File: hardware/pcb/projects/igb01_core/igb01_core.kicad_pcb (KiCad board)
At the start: 2 copper layers, 80 x 80 mm, 115 parts, among them J1 BAT_CON, J10 STMP157_GPIO2, J11 STMP157_GPIO3, J12 JTAG, J13 STMP157_GPIO4, J14 Micro_SD_Card, J15 PWR_ON_CON, J16 STMP157_GPIO5, J17 USB_CONN, J18 FPA-VZA2-15-LF, J19 I2C, J2 STMP157_GPIO1, J20 STMP157_GPIO6, J21 Conn_01x13, J3 LEFT_CON, J4 RIGHT_CON, J5 IGB_PREV, J6 IGB_NEXT, J7 IGB2_NEXT, J8 IGB3_NEXT, J9 CAN, SW1 SW_DIP_x04, SW2 SW_Push, SW3 SW_Push, U1 SIT1050T, U2 TPS2041B, U3 W25Q128JVS, U4 AK4619

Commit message: update core board sch&pcb
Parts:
- C4, C6: footprint Capacitor_SMD:C_0805_2012Metric -> Capacitor_SMD:C_0402_1005Metric
- moved U2 67.3 mm to (132.2, 89.2)
- moved C6 66.0 mm to (128.1, 85.1)
- moved C8 63.5 mm to (129.9, 86.5)
- moved R20 62.9 mm to (129.0, 90.2)
- moved C7 60.5 mm to (133.3, 86.5), turned to 180 degrees
- moved R30 57.4 mm to (159.4, 126.8)
- moved R31 56.5 mm to (159.4, 127.8)
- moved C4 47.2 mm to (151.9, 98.5)
- moved R15 47.0 mm to (151.4, 100.0)
- moved R2 46.8 mm to (151.1, 85.7)
- moved R12 44.1 mm to (153.8, 99.5), turned to -90 degrees
- moved R3 42.4 mm to (128.1, 68.1)
- moved R4 39.2 mm to (131.6, 68.1), turned to 180 degrees
- moved R8 38.8 mm to (150.2, 68.1)
- moved R28 26.9 mm to (160.4, 129.9), turned to 90 degrees
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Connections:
- J10 pad 15: /USB_OTG_FS_ID -> unconnected-(J10-Pin_15-Pad15)
- J10 pad 30: /SPI2_MOSI -> unconnected-(J10-Pin_30-Pad30)
- J11 pad 18: /GPIO_CLOCK_OUT -> unconnected-(J11-Pin_18-Pad18)
- J11 pad 20: /GPIO_RESET_OUT -> unconnected-(J11-Pin_20-Pad20)
- J11 pad 40: /SPI4_NSS -> unconnected-(J11-Pin_40-Pad40)
- J13 pad 33: /UART7_RX -> unconnected-(J13-Pin_33-Pad33)
- J13 pad 35: /UART7_TX -> unconnected-(J13-Pin_35-Pad35)
- J16 pad 25: /SPI4_GPIO_CS1 -> unconnected-(J16-Pin_25-Pad25)
- J16 pad 27: /SPI4_SCK -> unconnected-(J16-Pin_27-Pad27)
- J16 pad 28: /SPI2_NSS -> unconnected-(J16-Pin_28-Pad28)
- J16 pad 29: /SPI4_MISO -> unconnected-(J16-Pin_29-Pad29)
- J16 pad 31: /SPI4_MOSI -> unconnected-(J16-Pin_31-Pad31)
- J17 pad 1: /USB1_D+ -> /USB2_D+
- J17 pad 2: /USB1_D- -> /USB2_D-
- J17 pad 5: /USB2_D+ -> /USB1_D+
- J17 pad 6: /USB2_D- -> /USB1_D-
- J2 pad 19: unconnected-(J2-Pin_19-Pad19) -> /SPI6_MISO
- J2 pad 23: unconnected-(J2-Pin_23-Pad23) -> /SPI6_NSS
- J2 pad 24: unconnected-(J2-Pin_24-Pad24) -> /SPI6_MOSI
- J2 pad 25: unconnected-(J2-Pin_25-Pad25) -> /GPIO1
- J2 pad 26: unconnected-(J2-Pin_26-Pad26) -> /SPI6_SCK
- J2 pad 30: unconnected-(J2-Pin_30-Pad30) -> /SPI2_MISO
- J2 pad 35: unconnected-(J2-Pin_35-Pad35) -> /SPI2_CS_GPIO
- J2 pad 37: unconnected-(J2-Pin_37-Pad37) -> /GPIO_CLOCK_OUT
- J2 pad 39: unconnected-(J2-Pin_39-Pad39) -> /GPIO_RESET_OUT
- J2 pad 40: unconnected-(J2-Pin_40-Pad40) -> /SPI2_MOSI
- J20 pad 10: unconnected-(J20-Pin_10-Pad10) -> /LCD_TP_RST
- J20 pad 12: /LCD_TP_RST -> /LCD_TP_INT
- J20 pad 14: /LCD_TP_INT -> /UART8_TX
- J20 pad 15: unconnected-(J20-Pin_15-Pad15) -> /UART8_RX
- J20 pad 36: unconnected-(J20-Pin_36-Pad36) -> /I2C1_SDA
- J20 pad 40: /I2C1_SDA -> unconnected-(J20-Pin_40-Pad40)
- J3 pad 10: /USART3_TX -> /USART4_TX
- J3 pad 12: /SPI4_GPIO_CS1 -> /GPIO1
- J3 pad 13: /SPI4_NSS -> /SPI6_NSS
- J3 pad 14: /SPI4_MOSI -> /SPI6_MOSI
- J3 pad 15: /SPI4_MISO -> /SPI6_MISO
- J3 pad 16: /SPI4_SCK -> /SPI6_SCK
- J3 pad 18: /SPI2_NSS -> /SPI2_CS_GPIO
- J3 pad 7: /USART1_RX -> /UART8_RX
- J3 pad 8: /USART1_TX -> /UART8_TX
- J3 pad 9: /USART3_RX -> /USART4_RX
- R10 pad 2: /UART7_RX -> /USART6_RX
- R3 pad 2: /USART4_RX -> /USART1_RX
- R4 pad 2: /USART4_TX -> /USART1_TX
- R5 pad 2: /USART2_TX -> /USART3_TX
- R6 pad 2: /USART2_RX -> /USART3_RX
- R7 pad 2: /USART6_TX -> /USART2_TX
- R8 pad 2: /USART6_RX -> /USART2_RX
- R9 pad 2: /UART7_TX -> /USART6_TX
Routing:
- net +5V: track 43.2 -> 98.5 mm, vias 0 -> 2
- net Net-(J9-Pin_1): track 0.00 -> 52.1 mm, vias 0 -> 2
- net Net-(J9-Pin_2): track 0.00 -> 49.1 mm, vias 0 -> 2
- net +3.3V: track 195.0 -> 233.7 mm, vias 11 -> 13
- net /I2C4_SDA: track 0.00 -> 36.7 mm
- net /I2C4_SCL: track 0.00 -> 36.5 mm, vias 0 -> 2
- net VBUS: track 0.00 -> 36.4 mm, vias 0 -> 2
- net /AXP_PWR_ON: track 0.00 -> 35.5 mm, vias 0 -> 2
- net /SPI2_SCK: track 0.00 -> 33.2 mm, vias 0 -> 1
- net Net-(J17-Pin_3): track 0.00 -> 29.9 mm
- net /SPI2_MISO: track 0.00 -> 24.3 mm, vias 0 -> 1
- net +BATT: track 0.00 -> 22.6 mm
- net /GPIO_RESET_OUT: track 0.00 -> 21.0 mm
- net /GPIO_CLOCK_OUT: track 0.00 -> 20.5 mm
- net /USB_OTG_FS_D-: track 0.00 -> 19.2 mm, vias 0 -> 2
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
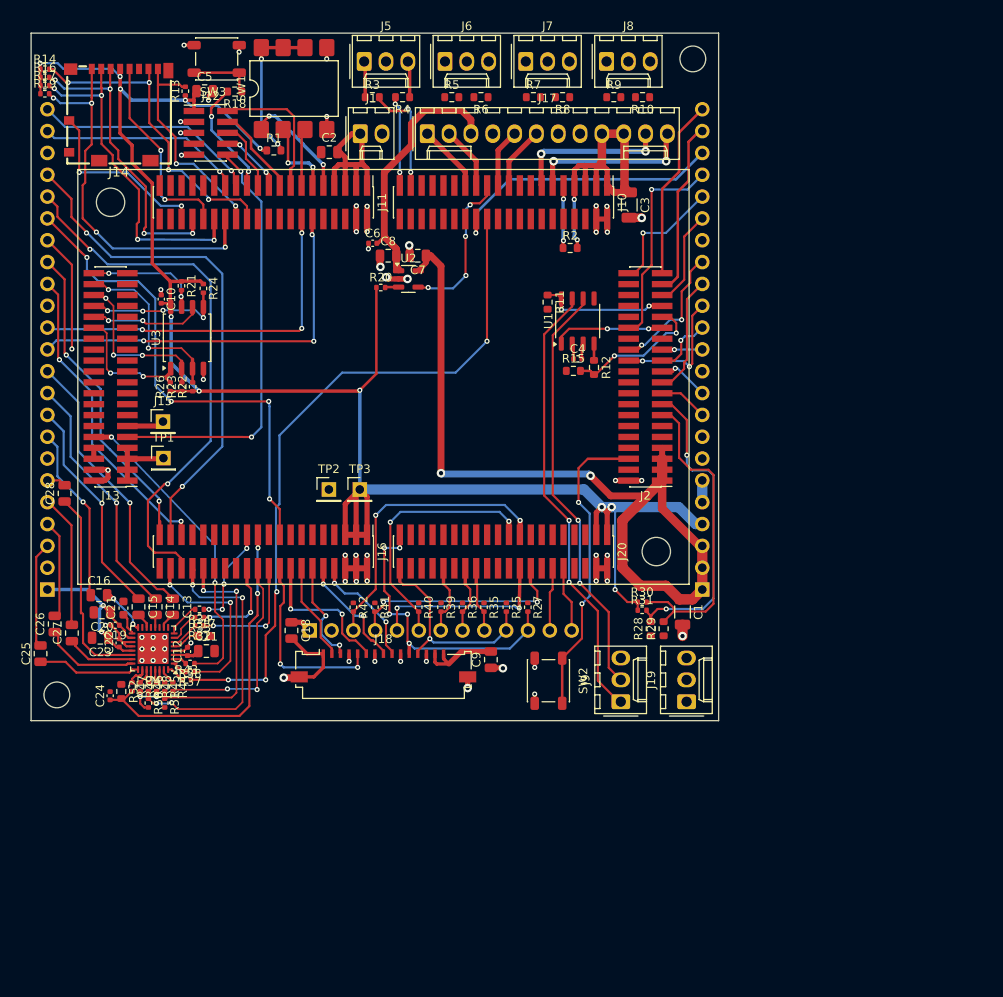
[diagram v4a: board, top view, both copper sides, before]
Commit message: connect all pads for core pcb
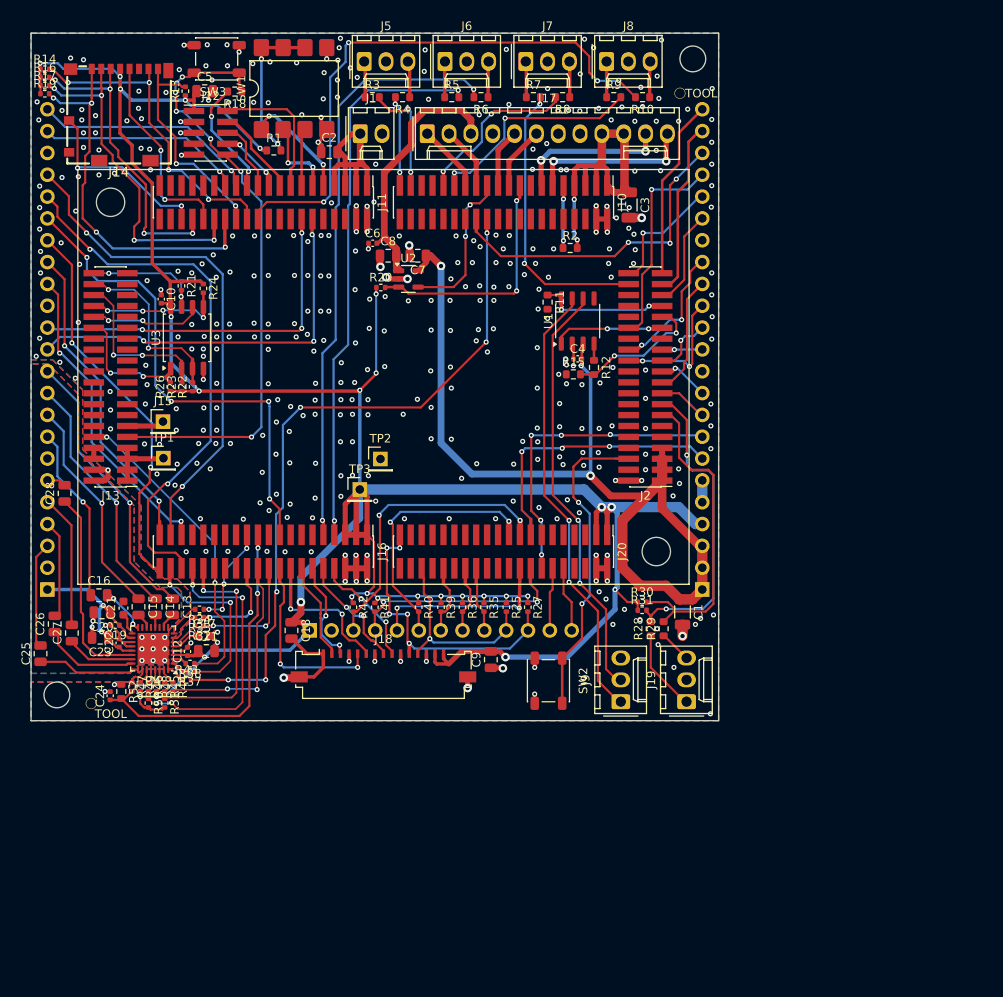
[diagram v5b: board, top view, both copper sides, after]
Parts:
- added REF**: JLC_TOOL_HOLE, kicadlib:JLC_TOOL_HOLE, F.Cu at (163.8, 67.7)
- added REF**: JLC_TOOL_HOLE, kicadlib:JLC_TOOL_HOLE, F.Cu at (95.3, 138.7)
- moved TP2 6.97 mm to (129.0, 110.2)
- moved R15 0.40 mm to (151.4, 100.3)
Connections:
- J16 pad 26: /SPI2_MISO -> unconnected-(J16-Pin_26-Pad26)
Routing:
- net +3.3V: track 233.7 -> 329.4 mm, vias 13 -> 27
- net /USART3_RX: track 0.00 -> 69.0 mm, vias 0 -> 2
- net /USART6_RX: track 0.00 -> 65.0 mm, vias 0 -> 4
- net /USART3_TX: track 0.00 -> 64.7 mm, vias 0 -> 2
- net /UART8_TX: track 0.00 -> 35.8 mm, vias 0 -> 5
- net /USART2_TX: track 0.00 -> 33.1 mm, vias 0 -> 2
- net /UART8_RX: track 0.00 -> 31.9 mm, vias 0 -> 3
- net /SDMMC3_D2: track 13.8 -> 45.2 mm, vias 1 -> 2
- net /USB1_OC_DETECT: track 1.58 -> 27.7 mm, vias 0 -> 2
- net /USART6_TX: track 0.00 -> 25.8 mm, vias 0 -> 2
- net /USART2_RX: track 0.00 -> 19.9 mm, vias 0 -> 2
- net /NRST: track 57.0 -> 70.6 mm, vias 2 -> 6
- net +5V: track 98.5 -> 110.4 mm, vias 2 -> 3
- net Net-(J19-Pin_1): track 0.00 -> 9.31 mm
- net GND: track 87.3 -> 93.7 mm, vias 48 -> 391
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- added copper zone on B.Cu, net GND
- added copper zone on F.Cu, net GND
- added copper zone on B.Cu, net GNDA
- added copper zone on F.Cu, net GNDA
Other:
- board text added: "TOOL"

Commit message: core pcb ver0.1
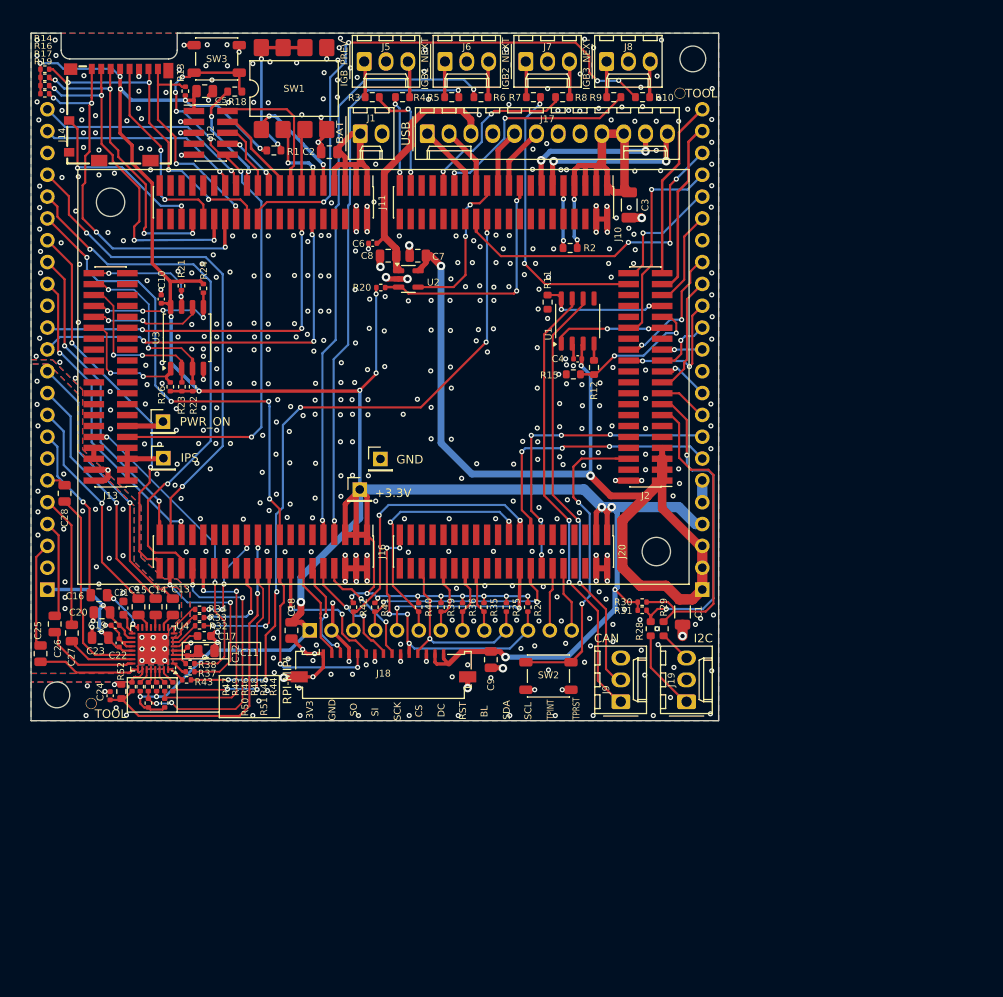
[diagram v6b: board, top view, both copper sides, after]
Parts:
- moved SW2 0.55 mm to (148.6, 135.4), turned to 0 degrees
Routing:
- net GND: track 93.7 -> 101.3 mm, vias 391 -> 468
- net GNDA: vias 12 -> 33
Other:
- outline, holes or cut-outs redrawn
- board text added: "+3.3V"
- board text added: "3V3"
- board text added: "BAT"
- board text added: "BL"
- board text added: "CAN"
- board text added: "CS"
- board text added: "DC"
- board text added: "GND"
- board text added: "I2C"
- board text added: "IGB01 CORE ver 0.1"
- board text added: "IGB1_NEXT"
- board text added: "IGB2_NEXT"
- board text added: "IGB3_NEXT"
- board text added: "IGB_PREV"
- board text added: "IPS"
- board text added: "PWR_ON"
- board text added: "RPI-MIPI"
- board text added: "RST"
- board text added: "SCK"
- board text added: "SCL"
- board text added: "SDA"
- board text added: "SI"
- board text added: "SO"
- board text added: "TPINT"
- board text added: "TPRST"
- board text added: "USB"

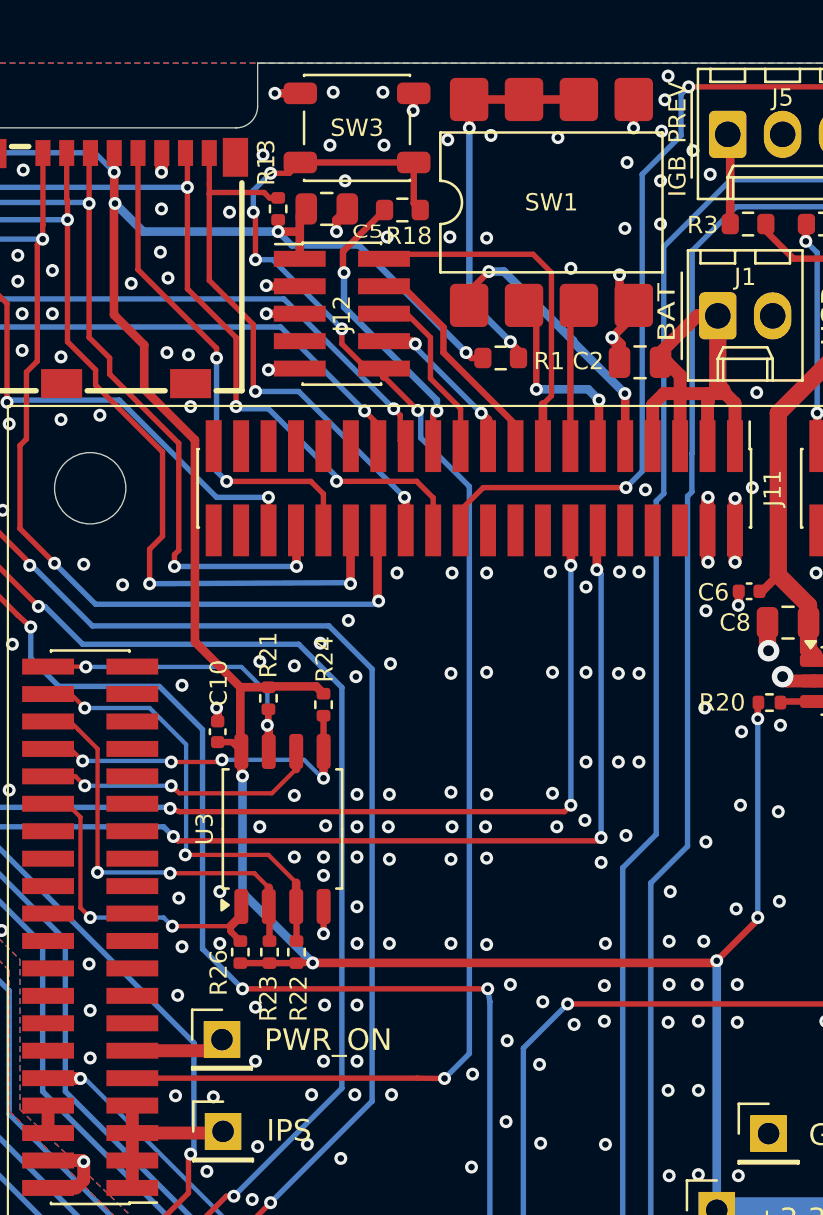
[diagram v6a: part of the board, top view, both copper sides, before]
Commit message: update igb01 core board & create gerber files
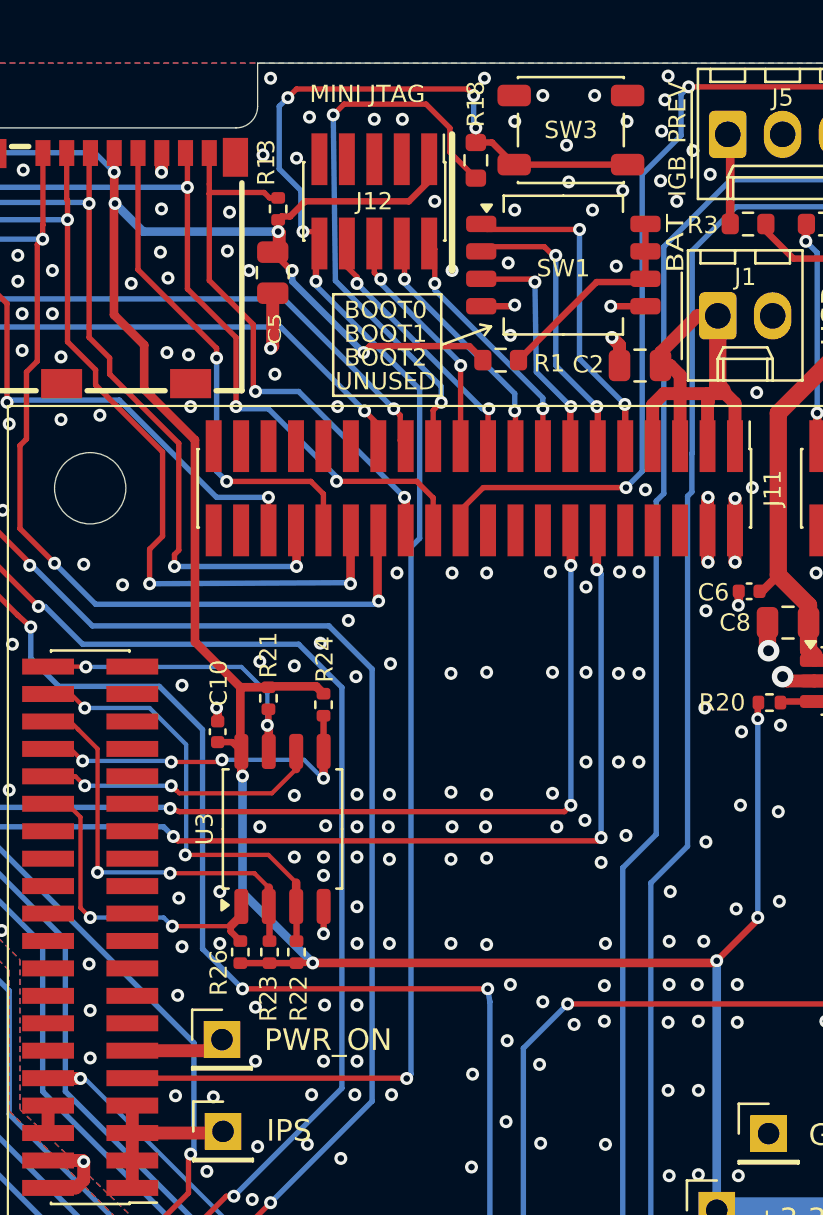
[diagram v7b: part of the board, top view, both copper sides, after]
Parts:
- SW1: footprint Package_DIP:SMDIP-8_W9.53mm -> custom:DIP_Switch_1.27mm_SMD
- moved SW3 9.90 mm to (119.8, 63.8)
- moved J12 5.41 mm to (110.8, 67.0), turned to -90 degrees
- moved R18 4.10 mm to (115.5, 65.2), turned to -90 degrees
- moved C5 3.87 mm to (106.0, 70.3), turned to -90 degrees
- moved SW1 2.95 mm to (119.5, 70.0), turned to 0 degrees
- moved C2 0.15 mm to (123.0, 74.7)
- moved R1 0.10 mm to (116.6, 74.4)
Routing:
- net /NJTRST: track 13.6 -> 26.4 mm
- net /NRST: track 70.6 -> 80.3 mm
- net Net-(R1-Pad2): track 17.8 -> 10.1 mm, vias 2 -> 0
- net +3.3V: track 329.4 -> 336.6 mm, vias 27 -> 28
- net GND: track 101.3 -> 95.9 mm, vias 468 -> 473
- net /JTDI: track 7.56 -> 12.6 mm
- net /BOOT1: track 8.65 -> 13.3 mm
- net /BOOT2: track 6.27 -> 10.8 mm, vias 0 -> 2
- net /JTMS-SWDIO: track 16.1 -> 11.6 mm, vias 0 -> 2
- net /JTDO-TRACESWO: track 7.16 -> 11.0 mm, vias 0 -> 2
- net /BOOT0: track 12.4 -> 15.6 mm
- net /JTCK-SWCLK: track 8.57 -> 11.6 mm, vias 0 -> 2
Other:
- board text added: "BOOT0"
- board text added: "BOOT1"
- board text added: "BOOT2"
- board text added: "MINI JTAG"
- board text added: "UNUSED"
